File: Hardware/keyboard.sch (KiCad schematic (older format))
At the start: 60 parts, among them M1 Tab, M10 O, M11 P, M12 Backspace, M13 Esc, M14 A, M15 S, M16 D, M17 F, M18 G, M19 H, M2 Q, M20 J, M21 K, M22 L, M23 ;, M24 ', M25 Shift, M26 Z, M27 X, M28 C, M29 V, M3 W, M30 B, M31 N, M32 M, M33 ,, M34 ., M35 /, M36 Enter, M37 Blnk, M38 Ctrl, M39 Alt, M4 E, M40 Super, M41 Down, M42 Space, M43 Up, M44 L_Ar, M45 D_Ar, M46 U_Ar, M47 R_Ar, M5 R, M6 T, M7 Y, M8 U, M9 I, U1 ROW_1, U2 ROW_2, U3 ROW_3, U4 ROW_4

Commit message: South-facing switch change
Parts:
- M1, M2, M3, M4, M5, M6: footprint Kailh_Pog:SW_Kailh_Choc_V1_1.00u -> Hardware:SW_Kailh_Choc_V1_1.00u
- M42: footprint Kailh_Pog:SW_Kailh_Choc_V1_2.00u -> Hardware:SW_Kailh_Choc_V1_2.00u
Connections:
- net ROW_1_0: now also U1.4 (GPB3); no longer U1.1 (GPB0)
- net ROW_1_1: now also U1.3 (GPB2); no longer U1.2 (GPB1)
- net ROW_1_10: now also U1.27 (GPA6); no longer U1.22 (GPA1)
- net ROW_1_11: now also U1.28 (GPA7); no longer U1.21 (GPA0)
- net ROW_1_2: now also U1.2 (GPB1); no longer U1.3 (GPB2)
- net ROW_1_3: now also U1.1 (GPB0); no longer U1.4 (GPB3)
- net ROW_1_4: now also U1.21 (GPA0); no longer U1.28 (GPA7)
- net ROW_1_5: now also U1.22 (GPA1); no longer U1.27 (GPA6)
- net ROW_1_6: now also U1.23 (GPA2); no longer U1.26 (GPA5)
- net ROW_1_7: now also U1.24 (GPA3); no longer U1.25 (GPA4)
- net ROW_1_8: now also U1.25 (GPA4); no longer U1.24 (GPA3)
- net ROW_1_9: now also U1.26 (GPA5); no longer U1.23 (GPA2)
- net ROW_2_0: now also U2.4 (GPB3); no longer U2.1 (GPB0)
- net ROW_2_1: now also U2.3 (GPB2); no longer U2.2 (GPB1)
- net ROW_2_10: now also U2.27 (GPA6); no longer U2.22 (GPA1)
- net ROW_2_11: now also U2.28 (GPA7); no longer U2.21 (GPA0)
- net ROW_2_2: now also U2.2 (GPB1); no longer U2.3 (GPB2)
- net ROW_2_3: now also U2.1 (GPB0); no longer U2.4 (GPB3)
- net ROW_2_4: now also U2.21 (GPA0); no longer U2.28 (GPA7)
- net ROW_2_5: now also U2.22 (GPA1); no longer U2.27 (GPA6)
- net ROW_2_6: now also U2.23 (GPA2); no longer U2.26 (GPA5)
- net ROW_2_7: now also U2.24 (GPA3); no longer U2.25 (GPA4)
- net ROW_2_8: now also U2.25 (GPA4); no longer U2.24 (GPA3)
- net ROW_2_9: now also U2.26 (GPA5); no longer U2.23 (GPA2)
- net ROW_3_0: now also U3.4 (GPB3); no longer U3.1 (GPB0)
- net ROW_3_1: now also U3.3 (GPB2); no longer U3.2 (GPB1)
- net ROW_3_10: now also U3.27 (GPA6); no longer U3.22 (GPA1)
- net ROW_3_11: now also U3.28 (GPA7); no longer U3.21 (GPA0)
- net ROW_3_2: now also U3.2 (GPB1); no longer U3.3 (GPB2)
- net ROW_3_3: now also U3.1 (GPB0); no longer U3.4 (GPB3)
- net ROW_3_4: now also U3.21 (GPA0); no longer U3.28 (GPA7)
- net ROW_3_5: now also U3.22 (GPA1); no longer U3.27 (GPA6)
- net ROW_3_6: now also U3.23 (GPA2); no longer U3.26 (GPA5)
- net ROW_3_7: now also U3.24 (GPA3); no longer U3.25 (GPA4)
- net ROW_3_8: now also U3.25 (GPA4); no longer U3.24 (GPA3)
- net ROW_3_9: now also U3.26 (GPA5); no longer U3.23 (GPA2)
- net ROW_4_0: now also U4.3 (GPB2); no longer U4.1 (GPB0)
- net ROW_4_10: now also U4.28 (GPA7); no longer U4.21 (GPA0)
- net ROW_4_2: now also U4.1 (GPB0); no longer U4.3 (GPB2)
- net ROW_4_3: now also U4.21 (GPA0); no longer U4.28 (GPA7)
- net ROW_4_4: now also U4.22 (GPA1); no longer U4.27 (GPA6)
- net ROW_4_5: now also U4.23 (GPA2); no longer U4.26 (GPA5)
- net ROW_4_6: now also U4.24 (GPA3); no longer U4.25 (GPA4)
- net ROW_4_7: now also U4.25 (GPA4); no longer U4.24 (GPA3)
- net ROW_4_8: now also U4.26 (GPA5); no longer U4.23 (GPA2)
- net ROW_4_9: now also U4.27 (GPA6); no longer U4.22 (GPA1)
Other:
- moved on the sheet: M25, M26, M27, M28, M29, M30, M31, M32, M33, M34, M35, M36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

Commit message: More rerouting.
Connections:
- net INT_0x4 is gone; now on net INT_0x0: C1.7 (PB08_A6_D6_TX)
- net +5V: now also R1.2, R2.1; no longer R1.1, R2.2
- net INT_0x0: no longer C1.1 (PA02_A0_D0)
- net INT_0x1: now also C1.6 (PA9_A5_D5_SCL); no longer C1.2 (PA4_A1_D1)
- net INT_0x2: now also C1.5 (PA8_A4_D4_SDA); no longer C1.3 (PA10_A2_D2)
- net SCL_: now also C1.1 (PA02_A0_D0), R1.1; no longer C1.6 (PA9_A5_D5_SCL), R1.2
- net SDA_: now also C1.2 (PA4_A1_D1), R2.2; no longer C1.5 (PA8_A4_D4_SDA), R2.1
- no-connect marks 32 -> 33
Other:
- moved on the sheet: R1, R2
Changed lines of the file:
@@
 Text Label 4600 1450 2    50   ~ 0
 INT_0x3
-Text Label 4600 1300 2    50   ~ 0
+Text Label 4600 1600 2    50   ~ 0
 INT_0x2
-Text Label 4600 1150 2    50   ~ 0
+Text Label 4600 1750 2    50   ~ 0
 INT_0x1
-Text Label 4600 1000 2    50   ~ 0
+Text Label 4600 1900 2    50   ~ 0
 INT_0x0
-Text Label 4150 1600 2    50   ~ 0
+Text Label 3950 1150 2    50   ~ 0
 SDA_
-Text Label 3950 1750 2    50   ~ 0
+Text Label 4150 1000 2    50   ~ 0
 SCL_
 Wire Wire Line
-	3950 1550 3950 1750
-Wire Wire Line
-	4150 1600 4150 1550
+	3950 950  3950 1150
+Wire Wire Line
+	4150 1000 4150 950
 $Comp
 L Device:R_Small R2
 U 1 1 617E595D
-P 4150 1450
-F 0 "R2" H 4091 1404 50  0000 R CNN
-F 1 "R_Small" H 4091 1495 50  0000 R CNN
-F 2 "Resistor_SMD:R_0603_1608Metric" H 4150 1450 50  0001 C CNN
-F 3 "~" H 4150 1450 50  0001 C CNN
-	1    4150 1450
-	-1   0    0    1
+P 3950 850
+F 0 "R2" H 3891 804 50  0000 R CNN
+F 1 "R_Small" H 3891 895 50  0000 R CNN
+F 2 "Resistor_SMD:R_0603_1608Metric" H 3950 850 50  0001 C CNN
+F 3 "~" H 3950 850 50  0001 C CNN
+	1    3950 850
+	1    0    0    -1
 $EndComp
 $Comp
 L Device:R_Small R1
 U 1 1 617E7D5B
-P 3950 1450
-F 0 "R1" H 3800 1500 50  0000 L CNN
-F 1 "R_Small" H 3600 1400 50  0000 L CNN
-F 2 "Resistor_SMD:R_0603_1608Metric" H 3950 1450 50  0001 C CNN
-F 3 "~" H 3950 1450 50  0001 C CNN
-	1    3950 1450
-	1    0    0    -1
+P 4150 850
+F 0 "R1" H 4000 900 50  0000 L CNN
+F 1 "R_Small" H 3800 800 50  0000 L CNN
+F 2 "Resistor_SMD:R_0603_1608Metric" H 4150 850 50  0001 C CNN
+F 3 "~" H 4150 850 50  0001 C CNN
+	1    4150 850
+	-1   0    0    1
 $EndComp
 $Comp
 L power:+5V #PWR011
 U 1 1 617E9B2D
-P 3950 1350
-F 0 "#PWR011" H 3950 1200 50  0001 C CNN
-F 1 "+5V" H 3965 1523 50  0000 C CNN
-F 2 "" H 3950 1350 50  0001 C CNN
-F 3 "" H 3950 1350 50  0001 C CNN
-	1    3950 1350
+P 3950 750
+F 0 "#PWR011" H 3950 600 50  0001 C CNN
+F 1 "+5V" H 3965 923 50  0000 C CNN
+F 2 "" H 3950 750 50  0001 C CNN
+F 3 "" H 3950 750 50  0001 C CNN
+	1    3950 750
 	1    0    0    -1
 $EndComp
@@
 L power:+5V #PWR012
 U 1 1 617EA5A5
-P 4150 1350
-F 0 "#PWR012" H 4150 1200 50  0001 C CNN
-F 1 "+5V" H 4165 1523 50  0000 C CNN
-F 2 "" H 4150 1350 50  0001 C CNN
-F 3 "" H 4150 1350 50  0001 C CNN
-	1    4150 1350
-	1    0    0    -1
-$EndComp
-Wire Wire Line
-	4600 1600 4150 1600
-Wire Wire Line
-	4600 1750 3950 1750
+P 4150 750
+F 0 "#PWR012" H 4150 600 50  0001 C CNN
+F 1 "+5V" H 4165 923 50  0000 C CNN
+F 2 "" H 4150 750 50  0001 C CNN
+F 3 "" H 4150 750 50  0001 C CNN
+	1    4150 750
+	1    0    0    -1
+$EndComp
+Wire Wire Line
+	4600 1000 4150 1000
+Wire Wire Line
+	4600 1150 3950 1150
 $Comp
 L power:GND #PWR020
@@
 NoConn ~ 4400 7650
 NoConn ~ 4400 7750
-Text Label 4600 1900 2    50   ~ 0
-INT_0x4
 $Comp
 L keyboard-rescue:SWITCH-SPST-2TV-SparkFun-Electromechanical-keyboard-rescue M38
@@
 Text Label 1650 7350 2    50   ~ 0
 ROW_3_0
+NoConn ~ 4600 1300
 $EndSCHEMATC

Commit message: Rerouting.
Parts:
- removed U4: ROW_4, MCP23017:SOIC127P1030X265-28N, symbol keyboard-rescue:MCP23017T-E_SO-MCP23017-keyboard-rescue
- C1: footprint RP2040:Seeeduino XIAO-MOUDLE14P-2.54-21X17.8MM -> Hardware:SeeeduinoXIAO-MOUDLE14P-2.54-21X17.8MM
- U1, U2, U3: footprint MCP23017:SOIC127P1030X265-28N -> Hardware:SOIC127P1030X265-28N
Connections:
- net ROW_1_0: now also U1.1 (GPB0); no longer U1.4 (GPB3)
- net ROW_1_1: now also U1.2 (GPB1); no longer U1.3 (GPB2)
- net ROW_1_2: now also U1.3 (GPB2); no longer U1.2 (GPB1)
- net ROW_1_3: now also U1.4 (GPB3); no longer U1.1 (GPB0)
- net ROW_2_0: now also U1.8 (GPB7); no longer U2.4 (GPB3)
- net ROW_2_1: now also U1.7 (GPB6); no longer U2.3 (GPB2)
- net ROW_2_2: now also U1.6 (GPB5); no longer U2.2 (GPB1)
- net ROW_2_3: now also U1.5 (GPB4); no longer U2.1 (GPB0)
- net ROW_3_0: now also U2.4 (GPB3); no longer U3.4 (GPB3)
- net ROW_3_1: now also U2.3 (GPB2); no longer U3.3 (GPB2)
- net ROW_3_10: now also U3.23 (GPA2); no longer U3.27 (GPA6)
- net ROW_3_11: now also U3.24 (GPA3); no longer U3.28 (GPA7)
- net ROW_3_2: now also U2.2 (GPB1); no longer U3.2 (GPB1)
- net ROW_3_3: now also U2.1 (GPB0); no longer U3.1 (GPB0)
- net ROW_3_4: now also U2.5 (GPB4); no longer U3.21 (GPA0)
- net ROW_3_5: now also U2.6 (GPB5); no longer U3.22 (GPA1)
- net ROW_3_6: now also U2.7 (GPB6); no longer U3.23 (GPA2)
- net ROW_3_7: now also U2.8 (GPB7); no longer U3.24 (GPA3)
- net ROW_3_8: now also U3.21 (GPA0); no longer U3.25 (GPA4)
- net ROW_3_9: now also U3.22 (GPA1); no longer U3.26 (GPA5)
- net ROW_4_0: now also U3.3 (GPB2)
- net ROW_4_1: now also U3.2 (GPB1)
- net ROW_4_10: now also U3.7 (GPB6)
- net ROW_4_2: now also U3.1 (GPB0)
- net ROW_4_3: now also U3.25 (GPA4)
- net ROW_4_4: now also U3.26 (GPA5)
- net ROW_4_5: now also U3.27 (GPA6)
- net ROW_4_6: now also U3.28 (GPA7)
- net ROW_4_7: now also U3.4 (GPB3)
- net ROW_4_8: now also U3.5 (GPB4)
- net ROW_4_9: now also U3.6 (GPB5)
- net INT_0x3: no longer names the net of C1.4 (PA11_A3_D3)
- no-connect marks 33 -> 17
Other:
- moved on the sheet: U3

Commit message: Moved location of I/O
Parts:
- removed H4: MountingHole, MountingHole:MountingHole_3.2mm_M3_Pad, symbol Mechanical:MountingHole
- M1, M10, M11, M12, M13, M14, M15, M16, M17, M18, M19, M2, M20, M21, M22, M23, M24, M25, M26, M27, M28, M29, M3, M30, M31, M32, M33, M34, M35, M36, M37, M38, M39, M4, M40, M41, M43, M44, M45, M46, M47, M5, M6, M7, M8, M9: footprint Hardware:SW_Kailh_Choc_V1_1.00u -> Hardware:SW_Cherry_MX_1.00u_PCB
- M42: footprint Hardware:SW_Kailh_Choc_V1_2.00u -> Hardware:SW_Cherry_MX_2.00u_PCB
- U1, U2, U3: footprint Hardware:SOIC127P1030X265-28N -> Package_DIP:DIP-28_W7.62mm
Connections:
- net INT_0x0: now also C1.5 (PA8_A4_D4_SDA); no longer C1.7 (PB08_A6_D6_TX)
- net INT_0x2: now also C1.7 (PB08_A6_D6_TX); no longer C1.5 (PA8_A4_D4_SDA)
- net ROW_1_0: now also U3.21 (GPA0); no longer U1.1 (GPB0)
- net ROW_1_1: now also U3.5 (GPB4); no longer U1.2 (GPB1)
- net ROW_1_10: now also U1.3 (GPB2); no longer U1.27 (GPA6)
- net ROW_1_11: now also U1.1 (GPB0); no longer U1.28 (GPA7)
- net ROW_1_2: now also U3.3 (GPB2); no longer U1.3 (GPB2)
- net ROW_1_3: now also U3.1 (GPB0); no longer U1.4 (GPB3)
- net ROW_1_4: now also U2.7 (GPB6); no longer U1.21 (GPA0)
- net ROW_1_5: now also U2.5 (GPB4); no longer U1.22 (GPA1)
- net ROW_1_6: now also U2.26 (GPA5); no longer U1.23 (GPA2)
- net ROW_1_7: now also U2.1 (GPB0); no longer U1.24 (GPA3)
- net ROW_1_8: now also U1.7 (GPB6); no longer U1.25 (GPA4)
- net ROW_1_9: now also U1.5 (GPB4); no longer U1.26 (GPA5)
- net ROW_2_0: now also U3.8 (GPB7); no longer U1.8 (GPB7)
- net ROW_2_1: now also U3.24 (GPA3); no longer U1.7 (GPB6)
- net ROW_2_10: now also U1.26 (GPA5); no longer U2.27 (GPA6)
- net ROW_2_11: now also U1.28 (GPA7); no longer U2.28 (GPA7)
- net ROW_2_2: now also U3.26 (GPA5); no longer U1.6 (GPB5)
- net ROW_2_3: now also U3.28 (GPA7); no longer U1.5 (GPB4)
- net ROW_2_4: now also U2.22 (GPA1); no longer U2.21 (GPA0)
- net ROW_2_5: now also U2.24 (GPA3); no longer U2.22 (GPA1)
- net ROW_2_6: now also U2.4 (GPB3); no longer U2.23 (GPA2)
- net ROW_2_7: now also U2.28 (GPA7); no longer U2.24 (GPA3)
- net ROW_2_8: now also U1.22 (GPA1); no longer U2.25 (GPA4)
- net ROW_2_9: now also U1.24 (GPA3); no longer U2.26 (GPA5)
- net ROW_3_0: now also U3.22 (GPA1); no longer U2.4 (GPB3)
- net ROW_3_1: now also U3.6 (GPB5); no longer U2.3 (GPB2)
- net ROW_3_10: now also U1.4 (GPB3); no longer U3.23 (GPA2)
- net ROW_3_11: now also U1.2 (GPB1); no longer U3.24 (GPA3)
- net ROW_3_2: now also U3.4 (GPB3); no longer U2.2 (GPB1)
- net ROW_3_3: now also U3.2 (GPB1); no longer U2.1 (GPB0)
- net ROW_3_4: now also U2.8 (GPB7); no longer U2.5 (GPB4)
- net ROW_3_6: now also U2.25 (GPA4); no longer U2.7 (GPB6)
- net ROW_3_7: now also U2.2 (GPB1); no longer U2.8 (GPB7)
- net ROW_3_8: now also U1.8 (GPB7); no longer U3.21 (GPA0)
- net ROW_3_9: now also U1.6 (GPB5); no longer U3.22 (GPA1)
- net ROW_4_0: now also U3.7 (GPB6); no longer U3.3 (GPB2)
- net ROW_4_1: now also U3.23 (GPA2); no longer U3.2 (GPB1)
- net ROW_4_10: now also U1.27 (GPA6); no longer U3.7 (GPB6)
- net ROW_4_2: now also U3.25 (GPA4); no longer U3.1 (GPB0)
- net ROW_4_3: now also U3.27 (GPA6); no longer U3.25 (GPA4)
- net ROW_4_4: now also U2.21 (GPA0); no longer U3.26 (GPA5)
- net ROW_4_5: now also U2.23 (GPA2); no longer U3.27 (GPA6)
- net ROW_4_6: now also U2.27 (GPA6); no longer U3.28 (GPA7)
- net ROW_4_7: now also U1.21 (GPA0); no longer U3.4 (GPB3)
- net ROW_4_8: now also U1.23 (GPA2); no longer U3.5 (GPB4)
- net ROW_4_9: now also U1.25 (GPA4); no longer U3.6 (GPB5)

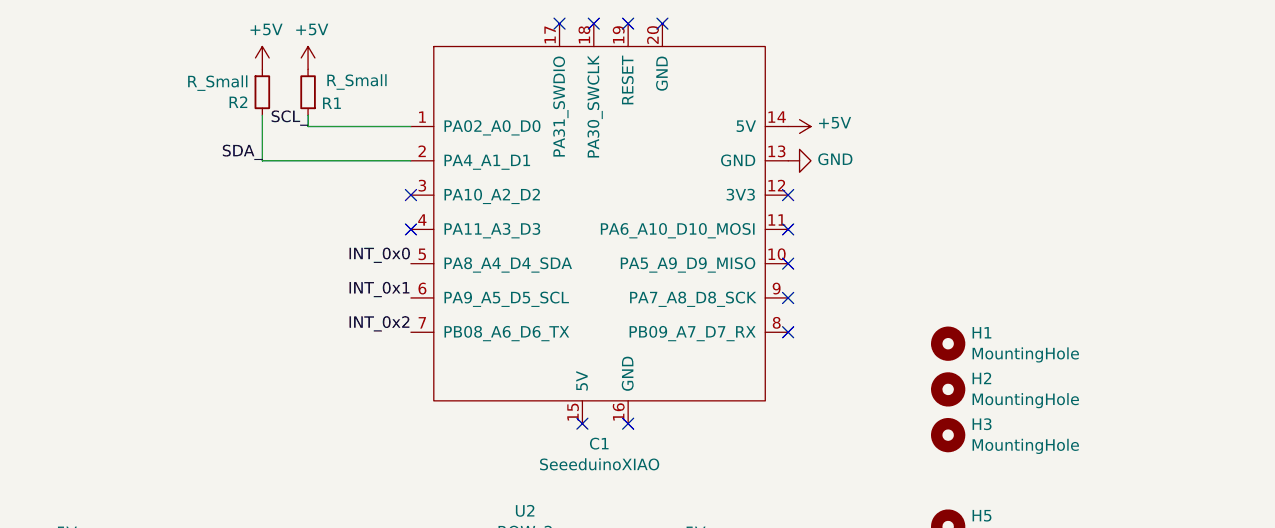
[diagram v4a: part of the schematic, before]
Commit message: Conversion to all through-hole components.
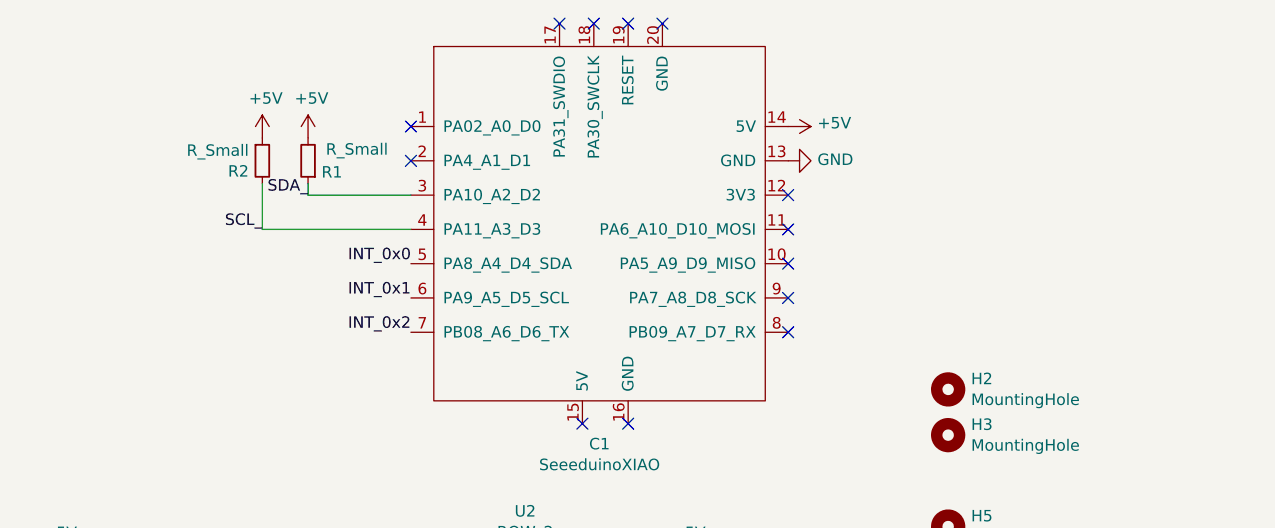
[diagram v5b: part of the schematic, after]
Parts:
- removed H1: MountingHole, MountingHole:MountingHole_3.2mm_M3_Pad, symbol Mechanical:MountingHole
- R1, R2: footprint Resistor_SMD:R_0603_1608Metric -> Resistor_THT:R_Axial_DIN0204_L3.6mm_D1.6mm_P7.62mm_Horizontal
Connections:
- net SCL_: now also C1.4 (PA11_A3_D3), R2.2; no longer C1.1 (PA02_A0_D0), R1.1
- net SDA_: now also C1.3 (PA10_A2_D2), R1.1; no longer C1.2 (PA4_A1_D1), R2.2
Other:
- moved on the sheet: R1, R2
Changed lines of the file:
@@
 Text Label 4600 1600 2    50   ~ 0
 INT_0x0
-Text Label 3950 1150 2    50   ~ 0
+Text Label 4150 1300 2    50   ~ 0
 SDA_
-Text Label 4150 1000 2    50   ~ 0
+Text Label 3950 1450 2    50   ~ 0
 SCL_
 Wire Wire Line
-	3950 950  3950 1150
-Wire Wire Line
-	4150 1000 4150 950
+	3950 1250 3950 1450
+Wire Wire Line
+	4150 1300 4150 1250
 $Comp
 L Device:R_Small R2
 U 1 1 617E595D
-P 3950 850
-F 0 "R2" H 3891 804 50  0000 R CNN
-F 1 "R_Small" H 3891 895 50  0000 R CNN
-F 2 "Resistor_SMD:R_0603_1608Metric" H 3950 850 50  0001 C CNN
-F 3 "~" H 3950 850 50  0001 C CNN
-	1    3950 850
+P 3950 1150
+F 0 "R2" H 3891 1104 50  0000 R CNN
+F 1 "R_Small" H 3891 1195 50  0000 R CNN
+F 2 "Resistor_THT:R_Axial_DIN0204_L3.6mm_D1.6mm_P7.62mm_Horizontal" H 3950 1150 50  0001 C CNN
+F 3 "~" H 3950 1150 50  0001 C CNN
+	1    3950 1150
 	1    0    0    -1
 $EndComp
@@
 L Device:R_Small R1
 U 1 1 617E7D5B
-P 4150 850
-F 0 "R1" H 4000 900 50  0000 L CNN
-F 1 "R_Small" H 3800 800 50  0000 L CNN
-F 2 "Resistor_SMD:R_0603_1608Metric" H 4150 850 50  0001 C CNN
-F 3 "~" H 4150 850 50  0001 C CNN
-	1    4150 850
+P 4150 1150
+F 0 "R1" H 4000 1200 50  0000 L CNN
+F 1 "R_Small" H 3800 1100 50  0000 L CNN
+F 2 "Resistor_THT:R_Axial_DIN0204_L3.6mm_D1.6mm_P7.62mm_Horizontal" H 4150 1150 50  0001 C CNN
+F 3 "~" H 4150 1150 50  0001 C CNN
+	1    4150 1150
 	-1   0    0    1
 $EndComp
@@
 L power:+5V #PWR011
 U 1 1 617E9B2D
-P 3950 750
-F 0 "#PWR011" H 3950 600 50  0001 C CNN
-F 1 "+5V" H 3965 923 50  0000 C CNN
-F 2 "" H 3950 750 50  0001 C CNN
-F 3 "" H 3950 750 50  0001 C CNN
-	1    3950 750
+P 3950 1050
+F 0 "#PWR011" H 3950 900 50  0001 C CNN
+F 1 "+5V" H 3965 1223 50  0000 C CNN
+F 2 "" H 3950 1050 50  0001 C CNN
+F 3 "" H 3950 1050 50  0001 C CNN
+	1    3950 1050
 	1    0    0    -1
 $EndComp
@@
 L power:+5V #PWR012
 U 1 1 617EA5A5
-P 4150 750
-F 0 "#PWR012" H 4150 600 50  0001 C CNN
-F 1 "+5V" H 4165 923 50  0000 C CNN
-F 2 "" H 4150 750 50  0001 C CNN
-F 3 "" H 4150 750 50  0001 C CNN
-	1    4150 750
+P 4150 1050
+F 0 "#PWR012" H 4150 900 50  0001 C CNN
+F 1 "+5V" H 4165 1223 50  0000 C CNN
+F 2 "" H 4150 1050 50  0001 C CNN
+F 3 "" H 4150 1050 50  0001 C CNN
+	1    4150 1050
 	1    0    0    -1
 $EndComp
 Wire Wire Line
-	4600 1000 4150 1000
-Wire Wire Line
-	4600 1150 3950 1150
+	4600 1300 4150 1300
+Wire Wire Line
+	4600 1450 3950 1450
 $Comp
 L power:GND #PWR020
@@
 $EndComp
 $Comp
-L Mechanical:MountingHole H1
-U 1 1 62184586
-P 6950 1950
-F 0 "H1" H 7050 1996 50  0000 L CNN
-F 1 "MountingHole" H 7050 1905 50  0000 L CNN
-F 2 "MountingHole:MountingHole_3.2mm_M3_Pad" H 6950 1950 50  0001 C CNN
-F 3 "~" H 6950 1950 50  0001 C CNN
-	1    6950 1950
-	1    0    0    -1
-$EndComp
-$Comp
 L Mechanical:MountingHole H3
 U 1 1 62184C5C
@@
 Text Label 4600 6150 0    50   ~ 0
 ROW_3_0
-NoConn ~ 4600 1300
+NoConn ~ 4600 1000
 $Comp
 L keyboard-rescue:MCP23017T-E_SO-MCP23017-keyboard-rescue U2
@@
 	1    0    0    -1
 $EndComp
-NoConn ~ 4600 1450
+NoConn ~ 4600 1150
 NoConn ~ 4400 4050
 $EndSCHEMATC
